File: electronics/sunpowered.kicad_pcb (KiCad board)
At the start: 2 copper layers, 60.2 x 42.7 mm, 18 parts, among them P1 CONN_01X04, P2 CONN_01X04, P3 CONN_01X04, Q1 CROWBAR, Q2 IRFR13N20D, U1 BSL316C

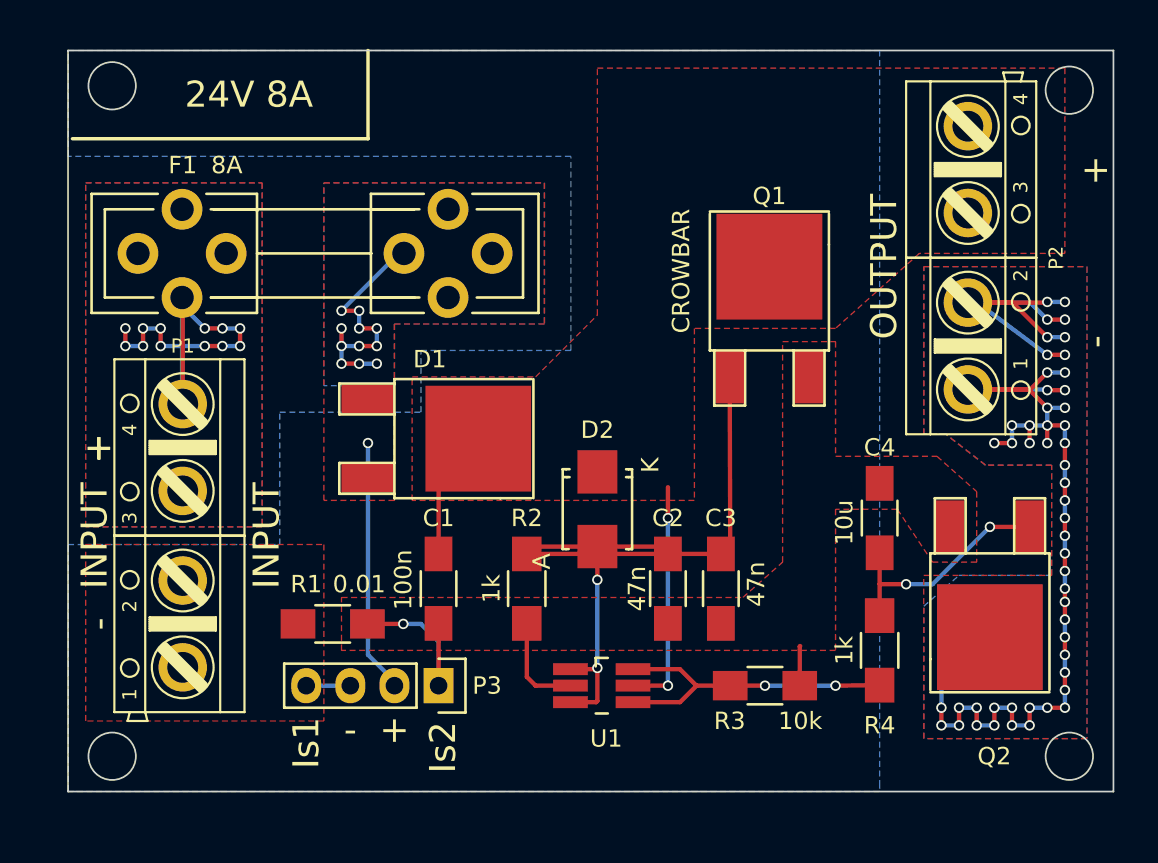
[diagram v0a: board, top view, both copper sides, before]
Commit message: normalized component values
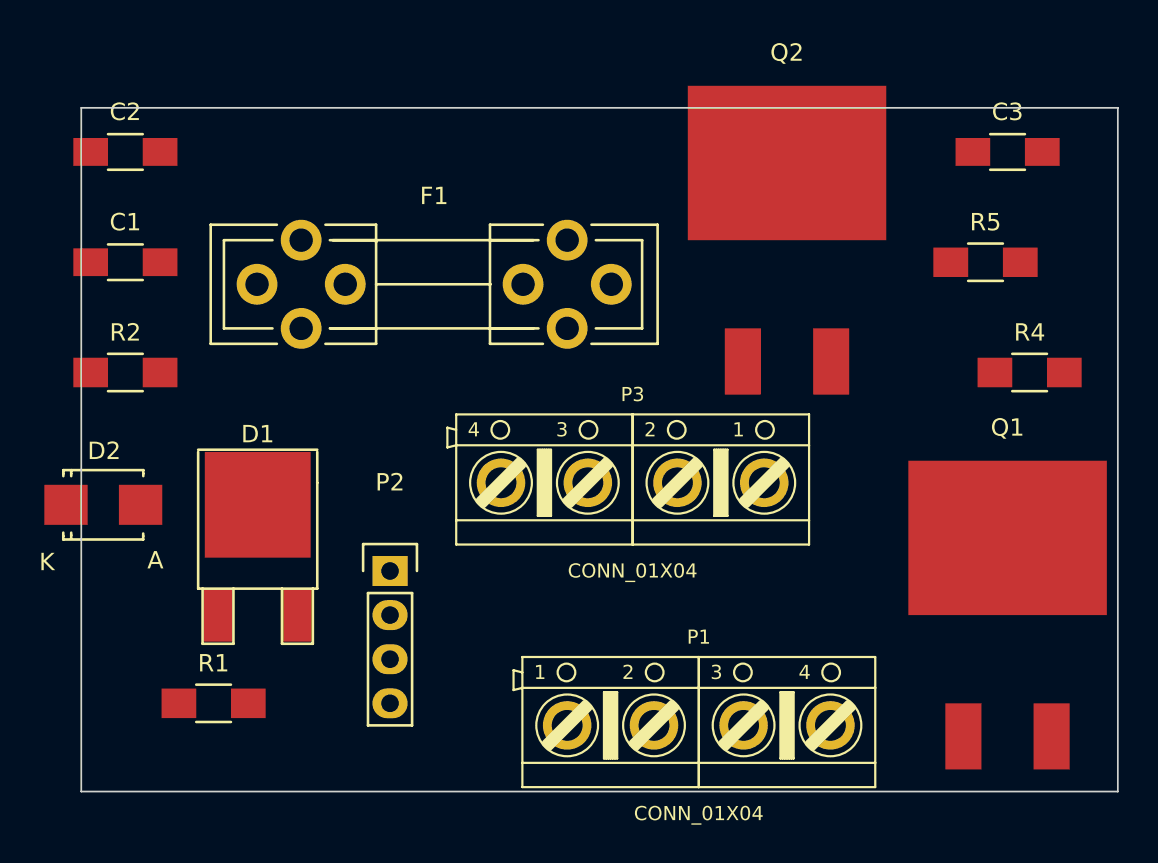
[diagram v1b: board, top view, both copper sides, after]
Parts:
- removed C4: 10u, Capacitors_SMD:C_1206_HandSoldering
- removed R3: 10k, Resistors_SMD:R_1206_HandSoldering
- removed REF**: Symbol_OSHW-Logo_SilkScreen_BIG, Symbols:Symbol_OSHW-Logo_SilkScreen_BIG
- removed U1: BSL316C, TO SOT SMD:TSOT-6-MK06A_Handsoldering
- added R5: 1k, Resistors_SMD:R_1206_HandSoldering, F.Cu at (154.9, 101.6)
- C3: value 47n -> 10u
- P2: footprint ab2_terminal_block:AB2_TB_04_RA_5MM_R-GRN -> Pin Headers:Pin_Header_Straight_1x04
- P3: footprint Pin Headers:Pin_Header_Straight_1x04 -> ab2_terminal_block:AB2_TB_04_RA_5MM_R-GRN
- Q1: value CROWBAR -> Q_PMOS_GDS; footprint TO SOT SMD:TO-252-2Lead -> cyplo's:D2PAK
- Q2: value IRFR13N20D -> Q_PMOS_GDS; footprint TO SOT SMD:TO-252-2Lead -> cyplo's:D2PAK
- R1: value 0.01 -> 0.01, 1W
- R2: value 1k -> 13k
- R4: value 1k -> 1M
- moved C2 40.1 mm to (105.4, 95.2), turned to 0 degrees
- moved P2 37.8 mm to (120.7, 119.4), turned to 0 degrees
- moved P1 31.7 mm to (138.4, 128.3), turned to 0 degrees
- moved C3 30.1 mm to (156.2, 95.2), turned to 0 degrees
- moved D2 28.4 mm to (104.1, 115.6), turned to 0 degrees
- moved R2 26.3 mm to (105.4, 108.0), turned to 0 degrees
- moved C1 26.0 mm to (105.4, 101.6), turned to 0 degrees
- moved Q1 23.3 mm to (156.2, 127.0)
- moved R4 18.2 mm to (157.5, 108.0), turned to 0 degrees
- moved Q2 16.3 mm to (143.5, 105.4), turned to 0 degrees
- moved P3 16.2 mm to (134.6, 114.3), turned to 0 degrees
- moved D1 12.0 mm to (113.0, 121.9), turned to 0 degrees
- moved R1 8.24 mm to (110.5, 127.0), turned to 0 degrees
- moved F1 7.08 mm to (123.2, 102.9)
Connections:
- C1 pad 1: /Input Measurement And Protection/RawPositive -> /Input Measurement And Protection/InputPower
- C3 pad 1: /Input Measurement And Protection/Overvoltage -> Net-(C3-Pad1)
- D1 pad 2: /Input Measurement And Protection/RawPositive -> /Input Measurement And Protection/InputPower
- D2 pad 1: /Input Measurement And Protection/RawPositive -> /Input Measurement And Protection/InputPower
- P2 pad 1: /Input Measurement And Protection/RawGround -> /Input Measurement And Protection/PanelCurrentSenseHigh
- P2 pad 2: /Input Measurement And Protection/RawGround -> /Input Measurement And Protection/PanelVoltageSense+
- P2 pad 3: /Input Measurement And Protection/RawPositive -> /Input Measurement And Protection/PanelCurrentSenseLow
- P2 pad 4: /Input Measurement And Protection/RawPositive -> /Input Measurement And Protection/PanelCurrentSenseLow
- P3 pad 2: /Input Measurement And Protection/PanelVoltageSense+ -> /Input Measurement And Protection/PanelCurrentSenseHigh
- P3 pad 3: /Input Measurement And Protection/PanelCurrentSenseLow -> /Input Measurement And Protection/RawPositive
- P3 pad 4: /Input Measurement And Protection/PanelCurrentSenseLow -> /Input Measurement And Protection/RawPositive
- Q1 pad 2: /Input Measurement And Protection/RawPositive -> /Input Measurement And Protection/VoltageOK
- Q2 pad 1: Net-(C4-Pad1) -> Net-(C3-Pad1)
- Q2 pad 2: /Input Measurement And Protection/RawGround -> /Input Measurement And Protection/InputPower
- Q2 pad 3: /Input Measurement And Protection/PanelCurrentSenseHigh -> /Input Measurement And Protection/RawPositive
- R4 pad 1: Net-(C4-Pad1) -> /Input Measurement And Protection/VoltageOK
- R4 pad 2: /Input Measurement And Protection/VoltageOK -> /Input Measurement And Protection/PanelCurrentSenseHigh
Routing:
- net /Input Measurement And Protection/RawGround: track 83.1 -> 0.00 mm, vias 51 -> 0
- net /Input Measurement And Protection/PanelVoltageSense+: track 59.3 -> 0.00 mm, vias 24 -> 0
- net /Input Measurement And Protection/Overvoltage: track 42.6 -> 0.00 mm, vias 2 -> 0
- net /Input Measurement And Protection/RawPositive: track 21.0 -> 0.00 mm, vias 2 -> 0
- net /Input Measurement And Protection/PanelCurrentSenseHigh: track 19.5 -> 0.00 mm, vias 1 -> 0
- net /Input Measurement And Protection/VoltageOK: track 18.6 -> 0.00 mm, vias 2 -> 0
- net Net-(C4-Pad1): track 13.6 -> 0.00 mm, vias 2 -> 0
- net /Input Measurement And Protection/PanelCurrentSenseLow: track 2.54 -> 0.00 mm
- removed copper zone on F.Cu, net /Input Measurement And Protection/PanelCurrentSenseHigh
- removed copper zone on B.Cu, net /Input Measurement And Protection/PanelCurrentSenseLow
- removed copper zone on F.Cu, net /Input Measurement And Protection/PanelCurrentSenseLow
- removed copper zone on B.Cu, net /Input Measurement And Protection/PanelVoltageSense+
- removed copper zone on F.Cu, net /Input Measurement And Protection/PanelVoltageSense+
- removed copper zone on B.Cu, net /Input Measurement And Protection/RawGround
- removed copper zone on F.Cu, net /Input Measurement And Protection/RawGround
- removed copper zone on F.Cu, net /Input Measurement And Protection/RawPositive
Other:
- board size 60.2 x 42.7 mm -> 59.7 x 39.4 mm
- board text removed: "+"
- board text removed: "-"
- board text removed: "24V 8A"
- board text removed: "24V 8A, rev A 2015-12, cyplo@cyplo.net"
- board text removed: "INPUT"
- board text removed: "Is1"
- board text removed: "Is2"
- board text removed: "OUTPUT"
- board text removed: "Sunpowered Input Protection and Measurement Board https://lab.cyplo.net/cyplo/sunpowered"
